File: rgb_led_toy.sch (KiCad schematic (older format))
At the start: 54 parts, among them IC1 AT168, IC2 MBI5168, IC3 MBI5168, IC4 MBI5168, P1 I2C, P2 PORTC, P3 FTDI, U1 MADW__TSOP38238

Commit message: V3.0 doodles.
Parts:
- removed D1, D2, D3, D4, D5, D6, D7, D8: RGB_SMD, symbol IMPOLUX_RGB_SMD
- removed D10, D11, D12, D13, D14, D15, D16, D9: LED, symbol LED
- removed IC2, IC3, IC4: MBI5168, symbol MBI5168
- removed R10, R11, R12, R13, R6, R7, R8, R9: R, symbol R
- removed R2: 10k, symbol R
- removed R3, R4, R5: 600R, symbol R
- removed RV1, RV2, RV3: 4k7, symbol POT
- added C10, C11: 4.7µF, symbol C
- added LED1, LED2, LED3, LED4, LED5, LED6, LED7, LED8: MADW__WS2812B, symbol MADW__WS2812B
- added NJ1: NET-JOIN, symbol JUMPER
- C4, C6, C8: value 100nF -> 4.7µF
- C5, C7, C9: value 10µF -> 4.7µF
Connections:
- net GND: now also NJ1.1; no longer C4.2, C5.2, C6.2, C7.2, C8.2, C9.2
- net VCC: now also C10.1, C11.1, LED1.1 (VCC), LED2.1 (VCC), LED3.1 (VCC), LED4.1 (VCC), LED5.1 (VCC), LED6.1 (VCC), LED7.1 (VCC), LED8.1 (VCC)
- net DATA: now reaches IC1.12 (PB0(ICP1))
- net DATA: now also LED1.4 (DIN)
- net LATCH: no longer names the net of IC1.14 (PB2(SS-/OC1B))
- net OE: no longer names the net of IC1.1 (PD3(INT1))
- net led0: no longer names the net of IC1.10 (PD6(AIN0))
- new net: LED1.2 (DOUT), LED2.4 (DIN)
- new net: LED2.2 (DOUT), LED3.4 (DIN)
- new net: LED3.2 (DOUT), LED4.4 (DIN)
- new net: LED4.2 (DOUT), LED5.4 (DIN)
- new net: LED5.2 (DOUT), LED6.4 (DIN)
- new net: LED6.2 (DOUT), LED7.4 (DIN)
- new net: LED7.2 (DOUT), LED8.4 (DIN)
- new net GNDPWR: C10.2, C11.2, C4.2, C5.2, C6.2, C7.2, C8.2, C9.2, LED1.3 (GND), LED2.3 (GND), LED3.3 (GND), LED4.3 (GND), LED5.3 (GND), LED6.3 (GND), LED7.3 (GND), LED8.3 (GND), NJ1.2
- no-connect marks 12 -> 14

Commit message: Might be a first working V3.0
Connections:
- net GND: no longer JP1.6 (GND), MH1.1, MH2.1, MH3.1, MH4.1, P1.3 (P3), P3.1
- net GNDPWR: now also JP1.6 (GND), P1.3 (P3), P3.1
- no-connect marks 14 -> 18
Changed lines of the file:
@@
 encoding utf-8
 Sheet 1 1
-Title "RGB LED Toy"
-Date "11 may 2012"
-Rev "2.1"
-Comp "2012 - My 2muF - blog.spitzenpfeil.org"
+Title "RGB LED Ring"
+Date "21 Sep 2013"
+Rev "3.0"
+Comp "2013 - blog.spitzenpfeil.org"
 Comment1 ""
 Comment2 ""
@@
 $EndDescr
 NoConn ~ 1550 2500
-Connection ~ 1400 6900
-Wire Wire Line
-	1250 6950 1250 6850
-Wire Wire Line
-	1250 6850 1400 6850
-Wire Wire Line
-	1400 6850 1400 7200
-Connection ~ 1400 7000
-Wire Wire Line
-	1450 7000 1400 7000
 Wire Wire Line
 	1450 2200 1550 2200
@@
 Wire Wire Line
 	1550 1200 1650 1200
-Wire Wire Line
-	1400 7200 1450 7200
-Wire Wire Line
-	1400 6900 1450 6900
-Wire Wire Line
-	1450 7100 1400 7100
-Connection ~ 1400 7100
 NoConn ~ 3950 2600
-$Comp
-L GND #PWR01
-U 1 1 4FA93F65
-P 1250 6950
-F 0 "#PWR01" H 1250 6950 30  0001 C CNN
-F 1 "GND" H 1250 6880 30  0001 C CNN
-F 2 "" H 1250 6950 60  0001 C CNN
-F 3 "" H 1250 6950 60  0001 C CNN
-	1    1250 6950
-	1    0    0    -1
-$EndComp
 Text Label 1450 2200 2    60   ~ 0
 INT0
@@
 NoConn ~ 1850 5600
 Text Label 1800 5700 2    60   ~ 0
-GND
+GNDP
 $Comp
 L CONN_6 P3
@@
 PC0
 Text Label 1200 5250 0    60   ~ 0
-GND
+GNDP
 Text Label 1200 5150 0    60   ~ 0
 VCC
@@
 MOSI
 Text Label 1950 6450 0    60   ~ 0
-GND
+GNDP
 Text Label 1950 6250 0    60   ~ 0
 VCC
@@
 Wire Wire Line
 	3650 6000 3650 6150
+Text Label 3850 5400 0    60   ~ 0
+GNDP
+NoConn ~ 1450 6900
+NoConn ~ 1450 7000
+NoConn ~ 1450 7100
+NoConn ~ 1450 7200
 $EndSCHEMATC

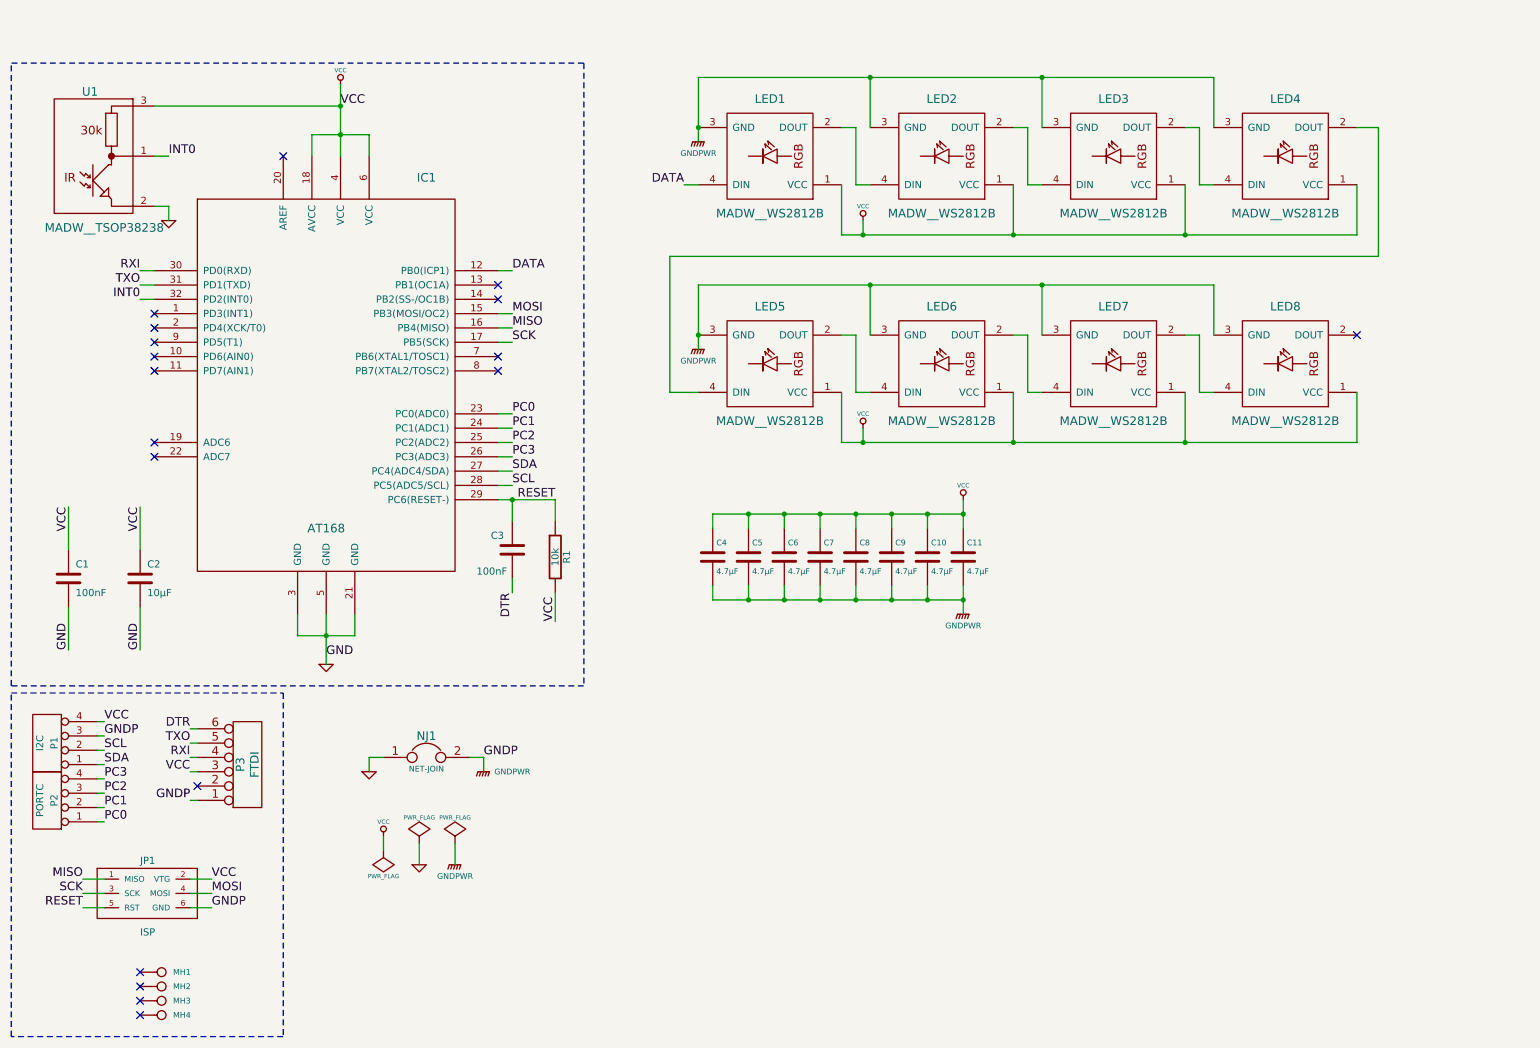
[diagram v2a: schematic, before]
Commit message: LED-string now goes clockwise. Added 1.27mm headers for all MCU pins.
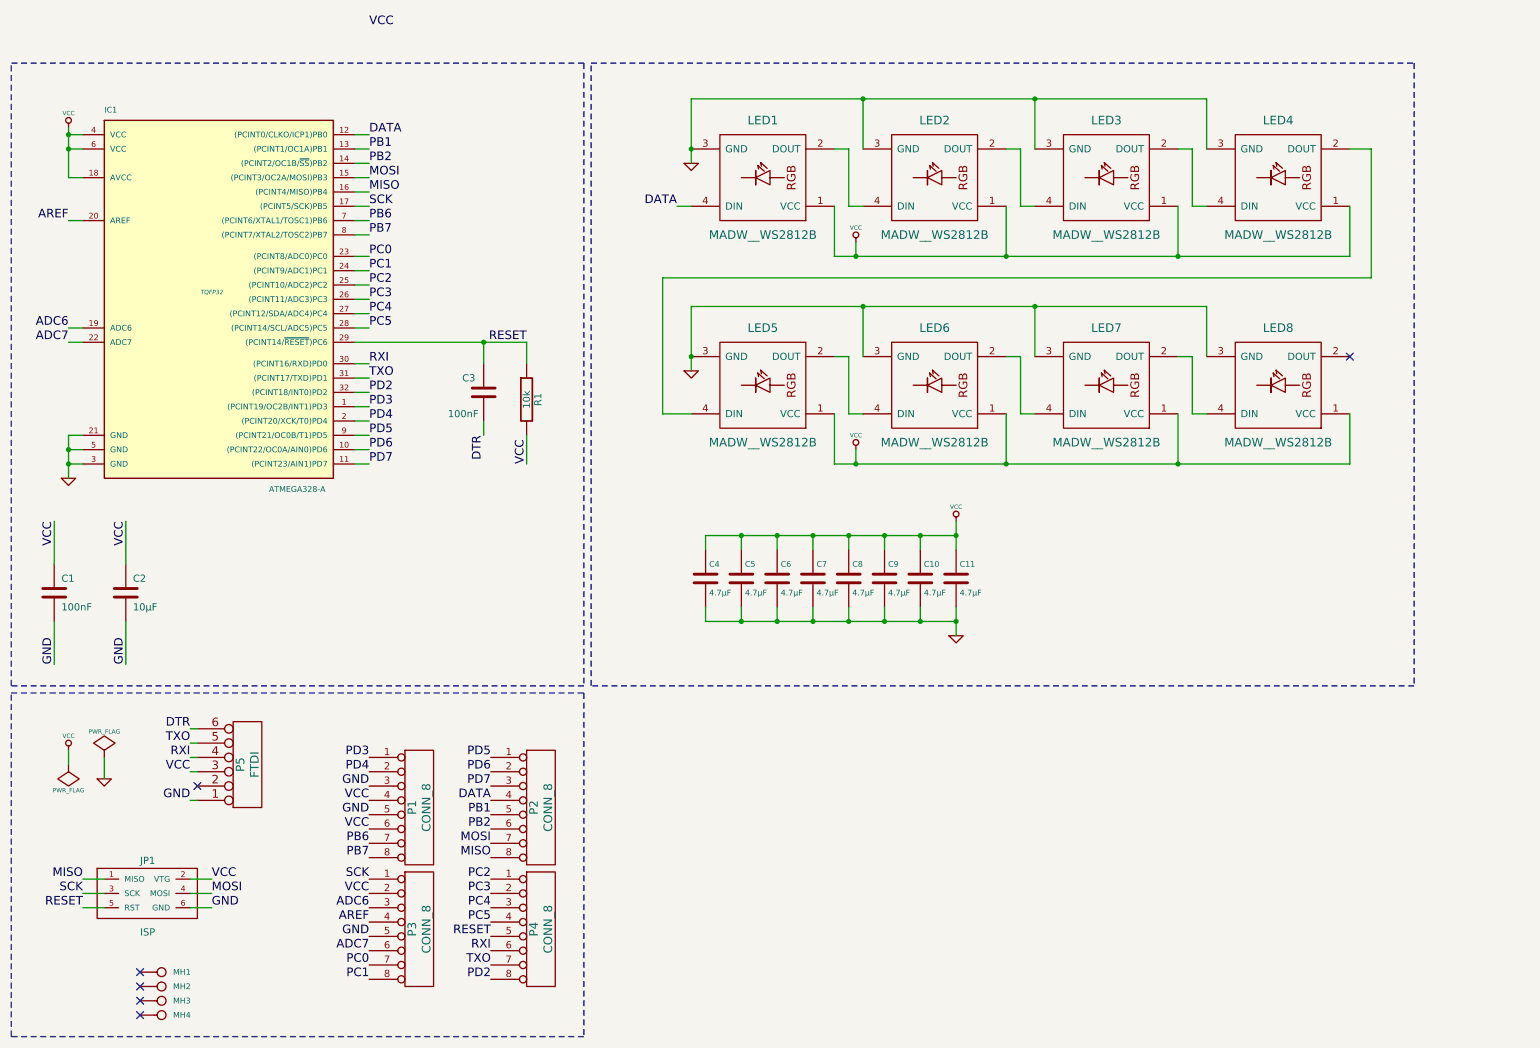
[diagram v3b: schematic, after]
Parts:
- removed IC1: AT168, symbol ATMEGA8_168_328_TQFP
- removed NJ1: NET-JOIN, symbol JUMPER
- removed P1: I2C, symbol CONN_4
- removed P2: PORTC, symbol CONN_4
- removed U1: MADW__TSOP38238, symbol MADW__TSOP38238
- added IC1: ATMEGA328-A, TQFP32, symbol ATMEGA328-A
- added P1, P2, P3, P4: CONN_8, symbol CONN_8
- renumbered P3 to P5
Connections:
- net GNDPWR is gone; now on net GND: C10.2, C11.2, C4.2, C5.2, C6.2, C7.2, C8.2, C9.2, JP1.6 (GND), LED1.3 (GND), LED2.3 (GND), LED3.3 (GND), LED4.3 (GND), LED5.3 (GND), LED6.3 (GND), LED7.3 (GND), LED8.3 (GND), P5.1
- net DATA: now also IC1.12 ((PCINT0/CLKO/ICP1)PB0), P2.4 (P4)
- net GND: now also IC1.21 (GND), IC1.3 (GND), IC1.5 (GND), P1.3 (P3), P1.5 (P5), P3.5 (P5)
- net MISO: now also IC1.16 ((PCINT4/MISO)PB4), P2.8 (P8)
- net MOSI: now also IC1.15 ((PCINT3/OC2A/MOSI)PB3), P2.7 (P7)
- net PC0: now also IC1.23 ((PCINT8/ADC0)PC0), P3.7 (P7)
- net PC1: now also IC1.24 ((PCINT9/ADC1)PC1), P3.8 (P8)
- net PC2: now also IC1.25 ((PCINT10/ADC2)PC2), P4.1 (P1)
- net PC3: now also IC1.26 ((PCINT11/ADC3)PC3), P4.2 (P2)
- net RESET: now also IC1.29 ((PCINT14/~RESET~)PC6), P4.5 (P5)
- net RXI: now also IC1.30 ((PCINT16/RXD)PD0), P4.6 (P6)
- net SCK: now also IC1.17 ((PCINT5/SCK)PB5), P3.1 (P1)
- net TXO: now also IC1.31 ((PCINT17/TXD)PD1), P4.7 (P7)
- net VCC: now also IC1.18 (AVCC), IC1.4 (VCC), IC1.6 (VCC), P1.4 (P4), P1.6 (P6), P3.2 (P2)
- new net ADC6: IC1.19 (ADC6), P3.3 (P3)
- new net ADC7: IC1.22 (ADC7), P3.6 (P6)
- new net AREF: IC1.20 (AREF), P3.4 (P4)
- new net PB1: IC1.13 ((PCINT1/OC1A)PB1), P2.5 (P5)
- new net PB2: IC1.14 ((PCINT2/OC1B/~SS~)PB2), P2.6 (P6)
- new net PB6: IC1.7 ((PCINT6/XTAL1/TOSC1)PB6), P1.7 (P7)
- new net PB7: IC1.8 ((PCINT7/XTAL2/TOSC2)PB7), P1.8 (P8)
- new net PC4: IC1.27 ((PCINT12/SDA/ADC4)PC4), P4.3 (P3)
- new net PC5: IC1.28 ((PCINT14/SCL/ADC5)PC5), P4.4 (P4)
- new net PD2: IC1.32 ((PCINT18/INT0)PD2), P4.8 (P8)
- new net PD3: IC1.1 ((PCINT19/OC2B/INT1)PD3), P1.1 (P1)
- new net PD4: IC1.2 ((PCINT20/XCK/T0)PD4), P1.2 (P2)
- new net PD5: IC1.9 ((PCINT21/OC0B/T1)PD5), P2.1 (P1)
- new net PD6: IC1.10 ((PCINT22/OC0A/AIN0)PD6), P2.2 (P2)
- new net PD7: IC1.11 ((PCINT23/AIN1)PD7), P2.3 (P3)
- no-connect marks 18 -> 6
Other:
- moved on the sheet: C1, C10, C11, C2, C3, C4, C5, C6, C7, C8, C9, LED1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

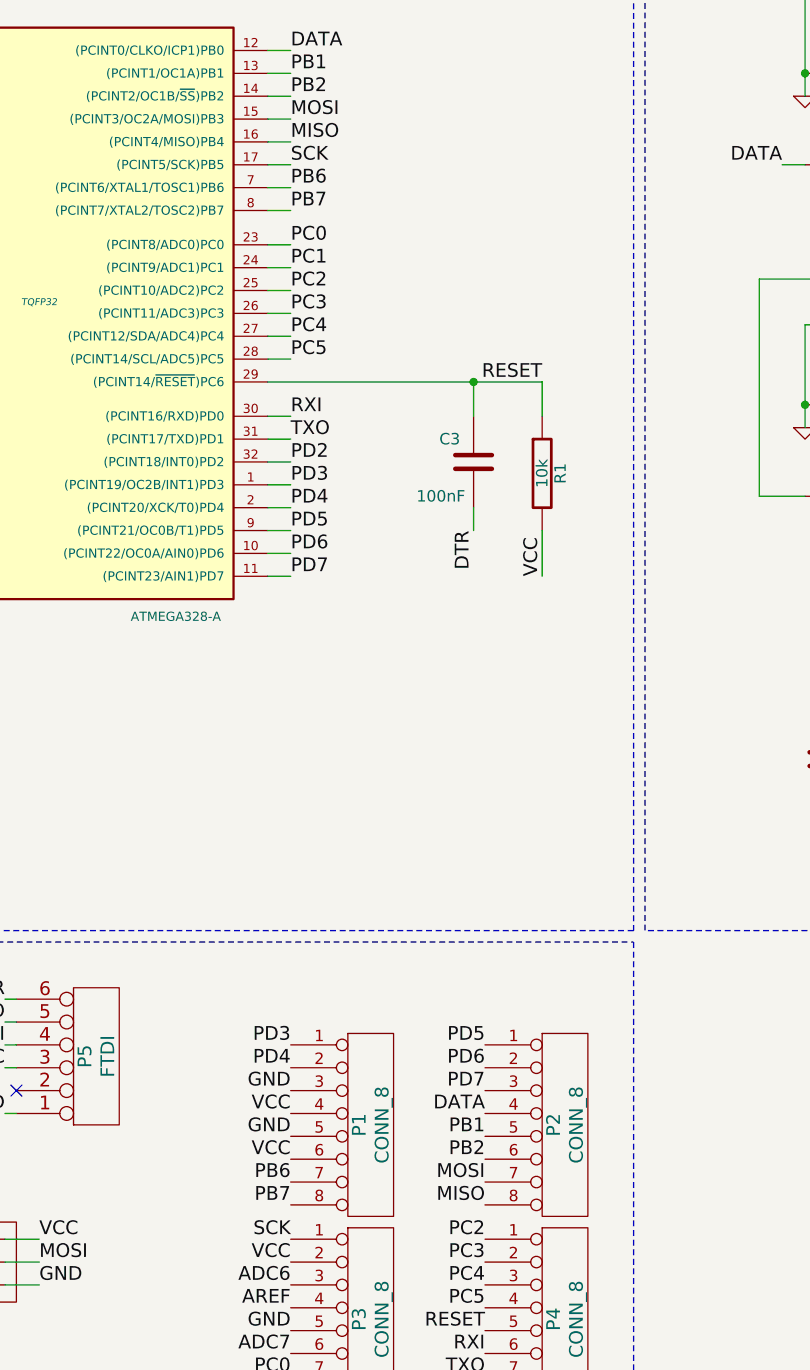
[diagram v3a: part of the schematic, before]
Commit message: Tweaks: silkscreen, copper p. cutouts, 8mil min trace width, 16MHz reso.
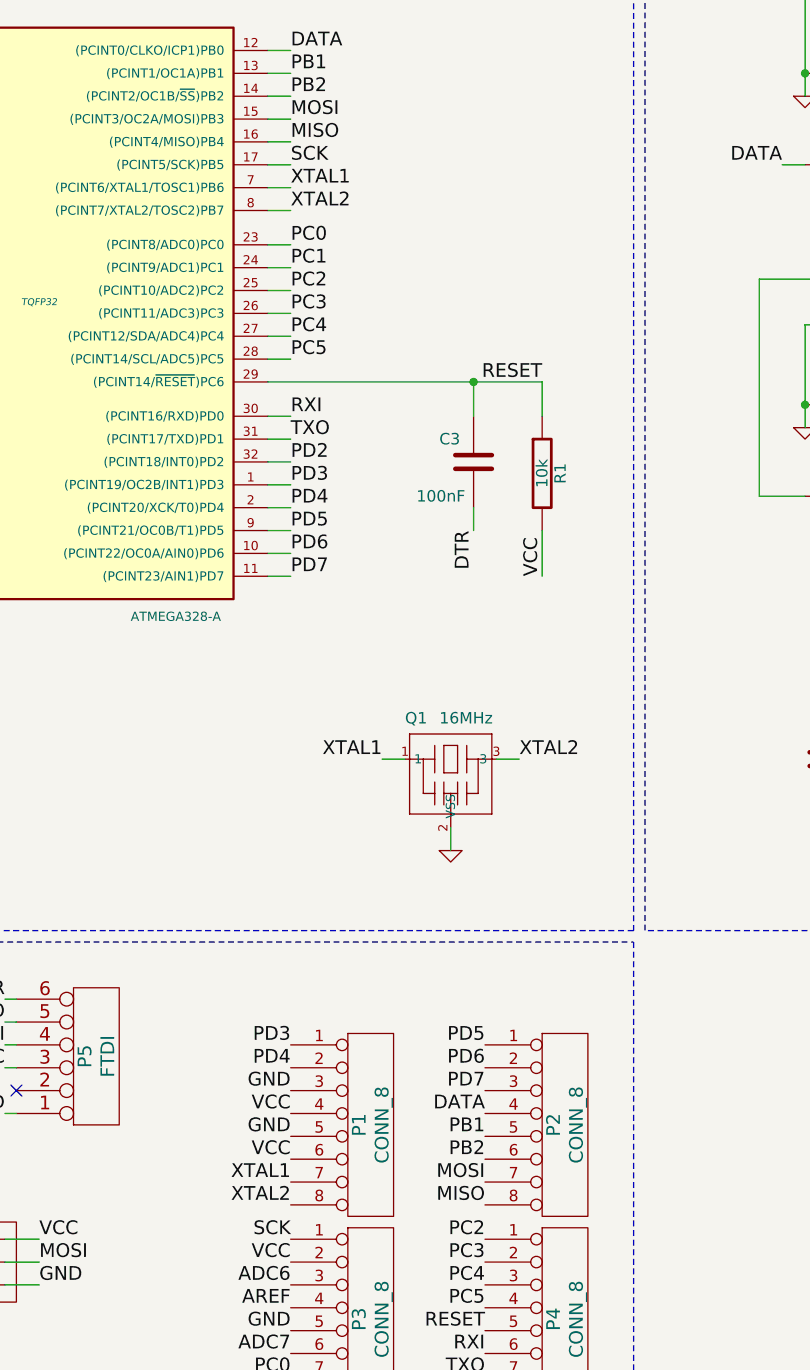
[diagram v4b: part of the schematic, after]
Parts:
- added Q1: 16MHz, murata-resonators-CSTLA_T, symbol CSTLA_T
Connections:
- net GND: now also Q1.2 (VSS)
- net PB6 renamed XTAL1
- net XTAL1: now also Q1.1
- net PB7 renamed XTAL2
- net XTAL2: now also Q1.3
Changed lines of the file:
@@
 LIBS:valves
 LIBS:atmel
+LIBS:murata-resonators
 LIBS:rgb_led_toy-cache
 EELAYER 24 0
@@
 VCC
 Text Label 3050 6000 2    60   ~ 0
-PB6
+XTAL1
 Text Label 3050 6100 2    60   ~ 0
-PB7
+XTAL2
 Text Label 3900 5400 2    60   ~ 0
 PD5
@@
 PB2
 Text Label 3050 1650 0    60   ~ 0
-PB6
+XTAL1
 Text Label 3050 1750 0    60   ~ 0
-PB7
+XTAL2
 Wire Wire Line
 	2950 1150 3050 1150
@@
 	1050 3250 950  3250
 Connection ~ 950  3250
+$Comp
+L CSTLA_T Q1
+U 1 1 523EC524
+P 3750 4150
+F 0 "Q1" H 3550 4300 50  0000 L BNN
+F 1 "16MHz" H 3700 4300 50  0000 L BNN
+F 2 "murata-resonators-CSTLA_T" H 3750 4300 50  0001 C CNN
+F 3 "" H 3750 4150 60  0000 C CNN
+	1    3750 4150
+	1    0    0    -1
+$EndComp
+$Comp
+L GND #PWR013
+U 1 1 523EC53D
+P 3750 4550
+F 0 "#PWR013" H 3750 4550 30  0001 C CNN
+F 1 "GND" H 3750 4480 30  0001 C CNN
+F 2 "" H 3750 4550 60  0000 C CNN
+F 3 "" H 3750 4550 60  0000 C CNN
+	1    3750 4550
+	1    0    0    -1
+$EndComp
+Wire Wire Line
+	3750 4450 3750 4550
+Text Label 3450 4150 2    60   ~ 0
+XTAL1
+Text Label 4050 4150 0    60   ~ 0
+XTAL2
+Wire Wire Line
+	3950 4150 4050 4150
+Wire Wire Line
+	3450 4150 3550 4150
 $EndSCHEMATC

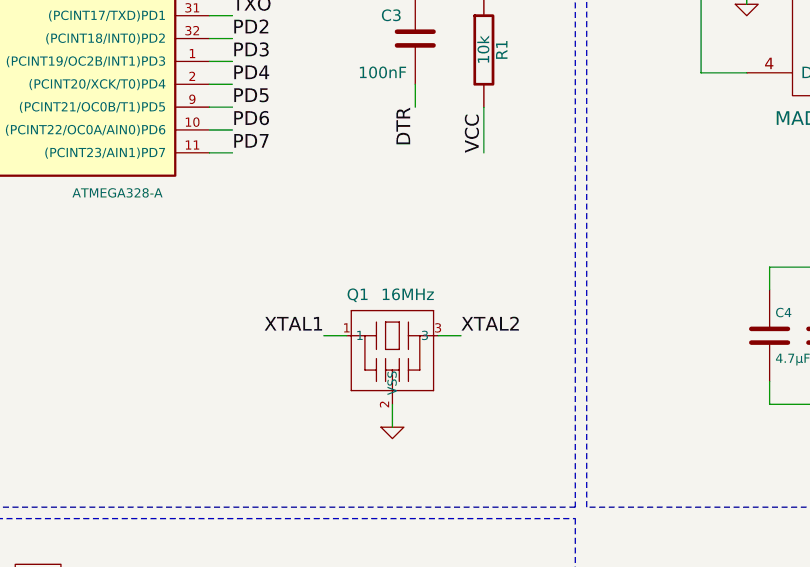
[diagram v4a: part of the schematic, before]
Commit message: Had to fix the resonator footprint (library part was off).
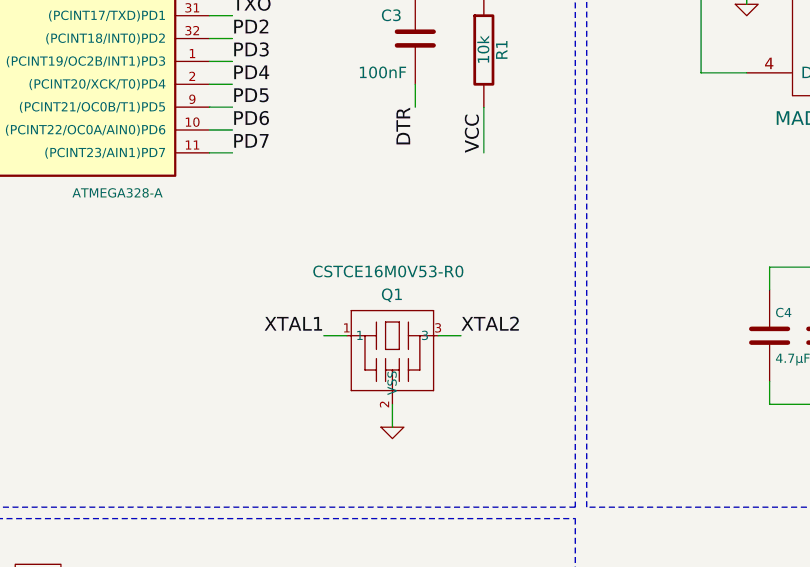
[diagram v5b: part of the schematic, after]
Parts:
- Q1: value 16MHz -> CSTCE16M0V53-R0
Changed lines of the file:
@@
 U 1 1 523EC524
 P 3750 4150
-F 0 "Q1" H 3550 4300 50  0000 L BNN
-F 1 "16MHz" H 3700 4300 50  0000 L BNN
+F 0 "Q1" H 3700 4300 50  0000 L BNN
+F 1 "CSTCE16M0V53-R0" H 3400 4400 50  0000 L BNN
 F 2 "murata-resonators-CSTLA_T" H 3750 4300 50  0001 C CNN
 F 3 "" H 3750 4150 60  0000 C CNN
